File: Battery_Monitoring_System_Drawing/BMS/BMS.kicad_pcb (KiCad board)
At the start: 2 copper layers, 62 parts, among them J1 SWD Pins, J2 INPUT 5V, J3 Micro_SD_Card_Det_Hirose_DM3AT, J4 Conn_01x04, J5 ACS INPUT, SW1 SW_Push_Dual, SW2 ESP RESET BUTTON, U1 STM32F101C8Tx, U2 AMS1117-3.3, U3 AMS1117-3.3, U4 ESP-12E, U5 ACS712xLCTR-30A, Y1 8M, Y2 32K

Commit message: Layout çizimi tamanlandı.
Layout çizimi ilk şablonu tamamlandı.
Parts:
- removed D4: SD CARD LED, LED_SMD:LED_0805_2012Metric
- removed R17: 68K, Resistor_SMD:R_0805_2012Metric
- C10, C14, C16, C18, C20, C21, C6, C7, C9, D3, J3, R13, R15, R2, R4, R5, R7, R8, R9, U2, U3: moved to B.Cu
- C19: value 100nF -> 10uF; moved to B.Cu
- C22: value 1nF -> 100nF
- C23: value 10uF -> 1nF
- J5: footprint Connector_Phoenix_MSTB:PhoenixContact_MSTBA_2,5_2-G_1x02_P5.00mm_Horizontal -> TerminalBlock_Phoenix:TerminalBlock_Phoenix_MKDS-1,5-2_1x02_P5.00mm_Horizontal
- R10: value 10K -> 12K; moved to B.Cu
- R11: value 12K -> 3.3K; moved to B.Cu
- R12: value 3.3K -> 12K; moved to B.Cu
- R14: value 12K -> 22K; moved to B.Cu
- R16: value 22K -> 68K; moved to B.Cu
- R6: value 470 -> 10K; moved to B.Cu
- Y1: footprint Crystal:Crystal_SMD_HC49-SD_HandSoldering -> Crystal:Crystal_SMD_HC49-SD
- moved R15 89.3 mm to (140.2, 105.4), turned to 180 degrees
- moved R16 85.1 mm to (140.2, 107.4)
- moved R12 79.4 mm to (143.6, 105.4), turned to 180 degrees
- moved TH1 72.0 mm to (155.7, 111.3), turned to 180 degrees
- moved R11 70.8 mm to (147.1, 107.4)
- moved JP3 67.0 mm to (151.9, 105.4), turned to 90 degrees
- moved R14 61.7 mm to (143.6, 107.4)
- moved R13 61.1 mm to (152.5, 108.8)
- moved J3 59.1 mm to (160.1, 87.9), turned to 270 degrees
- moved J5 58.5 mm to (162.1, 109.1)
- moved C21 58.4 mm to (177.0, 101.9), turned to 180 degrees
- moved SW2 58.2 mm to (171.0, 108.1)
- moved J4 54.5 mm to (146.8, 111.3), turned to 180 degrees
- moved D1 53.1 mm to (129.2, 104.1)
- moved U5 52.0 mm to (157.2, 98.6), turned to 90 degrees
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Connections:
- C20 pad 1: /ESP_RST -> +3.3VA
- C21 pad 1: GND -> /ESP_RST
- C21 pad 2: /Analog_Measurements/ACS_SUPPLY -> GND
- C22 pad 1: Net-(C22-Pad1) -> GND
- C22 pad 2: GND -> ACS_SUPPLY
- C23 pad 1: +3.3VA -> Net-(C23-Pad1)
- J3 pad 4: +3V3 -> +3.3VA
- JP3 pad 2: /Analog_Measurements/ACS_SUPPLY -> ACS_SUPPLY
- R10 pad 1: +3V3 -> CELL_3
- R10 pad 2: /SD_MOSI -> GND
- R11 pad 1: /Analog_Measurements/CELL_3 -> Net-(J4-Pad2)
- R11 pad 2: GND -> CELL_3
- R12 pad 1: Net-(J4-Pad2) -> CELL_2
- R12 pad 2: /Analog_Measurements/CELL_3 -> GND
- R13 pad 2: /Analog_Measurements/NTC -> NTC
- R14 pad 1: /Analog_Measurements/CELL_2 -> Net-(J4-Pad3)
- R14 pad 2: GND -> CELL_2
- R15 pad 1: Net-(J4-Pad3) -> CELL_1
- R15 pad 2: /Analog_Measurements/CELL_2 -> GND
- R16 pad 1: /Analog_Measurements/CELL_1 -> Net-(J4-Pad4)
- R16 pad 2: GND -> CELL_1
- R6 pad 2: Net-(D4-Pad2) -> /SD_MOSI
- R7 pad 1: +3V3 -> +3.3VA
- R7 pad 2: Net-(J3-Pad8) -> /SD_SCLK
- R8 pad 1: +3V3 -> +3.3VA
- R9 pad 1: +3V3 -> +3.3VA
- R9 pad 2: /SD_SCLK -> Net-(J3-Pad8)
- TH1 pad 1: /Analog_Measurements/NTC -> NTC
- U4 pad 3: +3.3VA -> +3V3
- U4 pad 8: +3.3VA -> +3V3
- U5 pad 6: Net-(C22-Pad1) -> Net-(C23-Pad1)
- U5 pad 7: /Analog_Measurements/ACS_OUT -> ACS_OUT
- U5 pad 8: /Analog_Measurements/ACS_SUPPLY -> ACS_SUPPLY
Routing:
- net +3V3: track 0.00 -> 146.5 mm, vias 0 -> 7
- net GND: track 0.00 -> 73.8 mm, vias 0 -> 48
- net +3.3VA: track 0.00 -> 55.8 mm
- net +5V: track 0.00 -> 53.7 mm
- net /ESP_RST: track 0.00 -> 35.7 mm, vias 0 -> 1
- net NRST: track 0.00 -> 33.0 mm, vias 0 -> 1
- net Net-(J3-Pad8): track 0.00 -> 32.8 mm
- net ESP_TX: track 0.00 -> 31.2 mm, vias 0 -> 2
- net NTC: track 0.00 -> 30.5 mm, vias 0 -> 1
- net ESP_RX: track 0.00 -> 28.4 mm, vias 0 -> 2
- net TEST_PIN: track 0.00 -> 25.1 mm
- net CELL_1: track 0.00 -> 22.7 mm, vias 0 -> 1
- net SWDIO: track 0.00 -> 22.5 mm, vias 0 -> 1
- net /SD_MISO: track 0.00 -> 21.9 mm, vias 0 -> 1
- net CELL_2: track 0.00 -> 20.3 mm, vias 0 -> 1
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- added copper zone on B.Cu, net GND
- added copper zone on F.Cu, net GND
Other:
- board outline added: 52.6 x 41.4 mm
- rule via_min_size: 0.4 -> 0.3

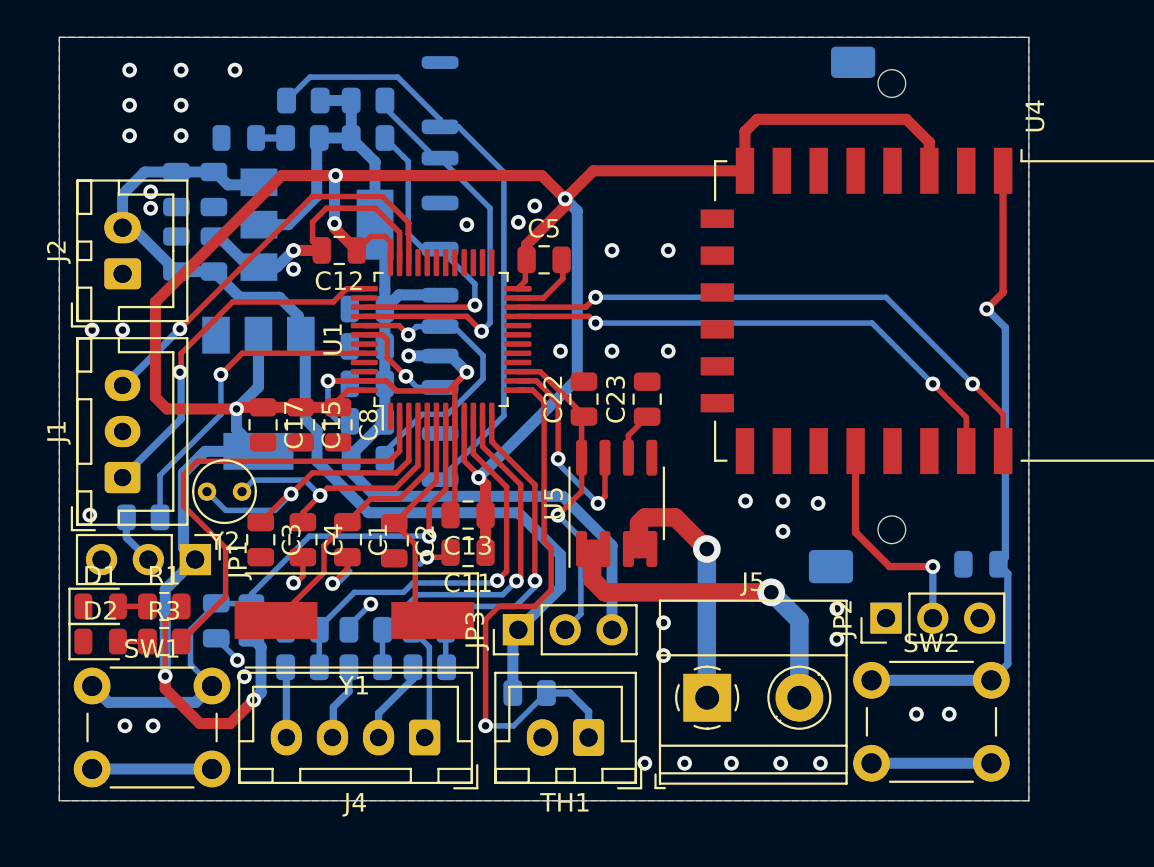
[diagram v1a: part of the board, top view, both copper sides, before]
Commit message: DRC hataları çözüldü.
DRC hataları çözüldü ve SD Card 3D görüntüsü eklendi.
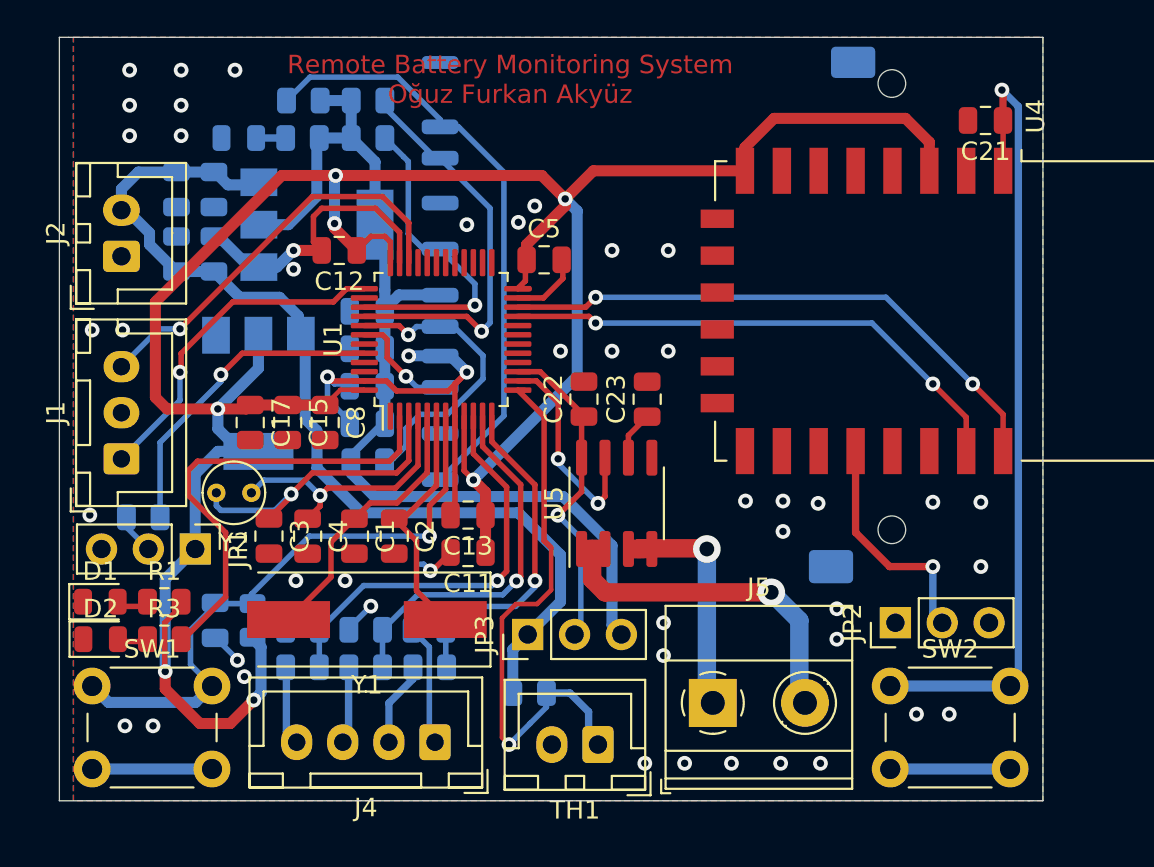
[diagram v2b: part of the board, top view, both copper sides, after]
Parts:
- C21: moved to F.Cu
- moved C21 24.1 mm to (177.2, 77.8)
- moved SW2 1.06 mm to (172.1, 108.5)
- moved J1 1.02 mm to (130.4, 96.1)
- moved J2 0.95 mm to (130.4, 85.2)
- moved C15 0.71 mm to (139.4, 94.2)
- moved C17 0.71 mm to (137.4, 94.2)
- moved C8 0.71 mm to (141.4, 94.2)
- moved Y1 0.68 mm to (143.7, 104.9)
- moved TH1 0.64 mm to (156.2, 111.6)
- moved J4 0.61 mm to (147.4, 111.5)
- moved JP1 0.57 mm to (134.4, 101.0)
- moved JP3 0.57 mm to (152.4, 105.7)
- moved JP2 0.57 mm to (172.3, 105.0)
- moved Y2 0.51 mm to (137.4, 98.0)
- moved C3 0.49 mm to (138.4, 100.3)
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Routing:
- net /ESP_RST: track 35.7 -> 43.8 mm
- net GND: track 73.8 -> 69.8 mm, vias 48 -> 49
- net Net-(J5-Pad1): track 15.3 -> 13.1 mm
- net SWCLK: track 19.4 -> 18.4 mm
- net OSC32_OUT: track 15.3 -> 14.6 mm
- net /ESP_IO0: track 12.2 -> 12.8 mm
- net OSC32_IN: track 17.2 -> 16.6 mm
- net Net-(JP1-Pad2): track 2.85 -> 2.27 mm
- net NTC: track 30.5 -> 30.0 mm
- net OSC_OUT: track 12.9 -> 13.4 mm
- net +3.3VA: track 55.8 -> 56.3 mm
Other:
- board size 52.6 x 41.4 mm -> 53.3 x 41.4 mm
- board text added: "Remote Battery Monitoring System Oğuz Furkan Akyüz"

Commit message: Düzenleme yapıldı.
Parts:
- moved C17 1.78 mm to (135.6, 94.2)
- moved C15 1.78 mm to (137.6, 94.2)
- moved C8 1.78 mm to (139.6, 94.2)
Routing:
- net +3V3: track 146.3 -> 151.0 mm
- net BOOT0: track 17.4 -> 18.1 mm
- net GND: vias 49 -> 51
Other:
- board text added: "Oğuz Furkan Akyüz - 2021"
- board text added: "Remote Battery Monitoring System"
- board text removed: "Remote Battery Monitoring System Oğuz Furkan Akyüz"

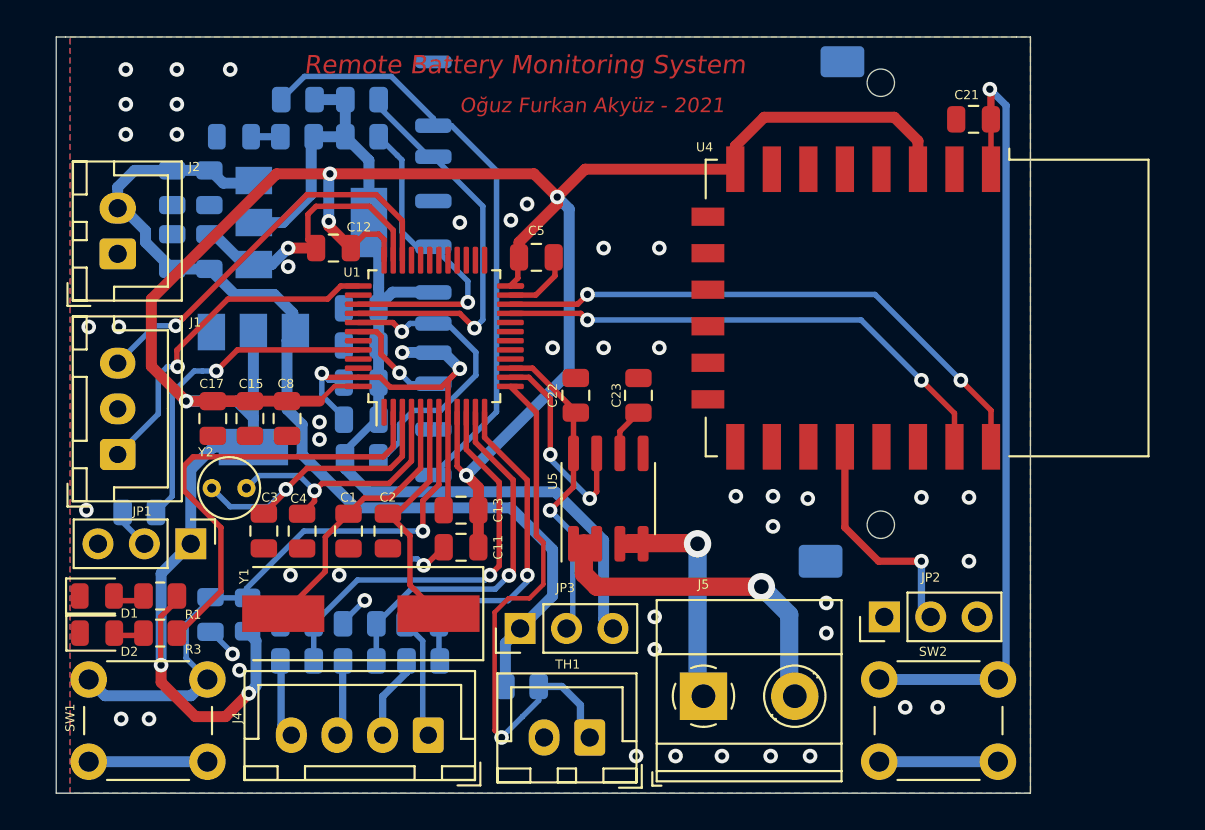
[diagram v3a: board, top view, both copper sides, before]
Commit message: Micro Sd kılıf eklendi.
Sd kart holder kılıfı micro sd kart soket kılıfı ile değiştirildi.
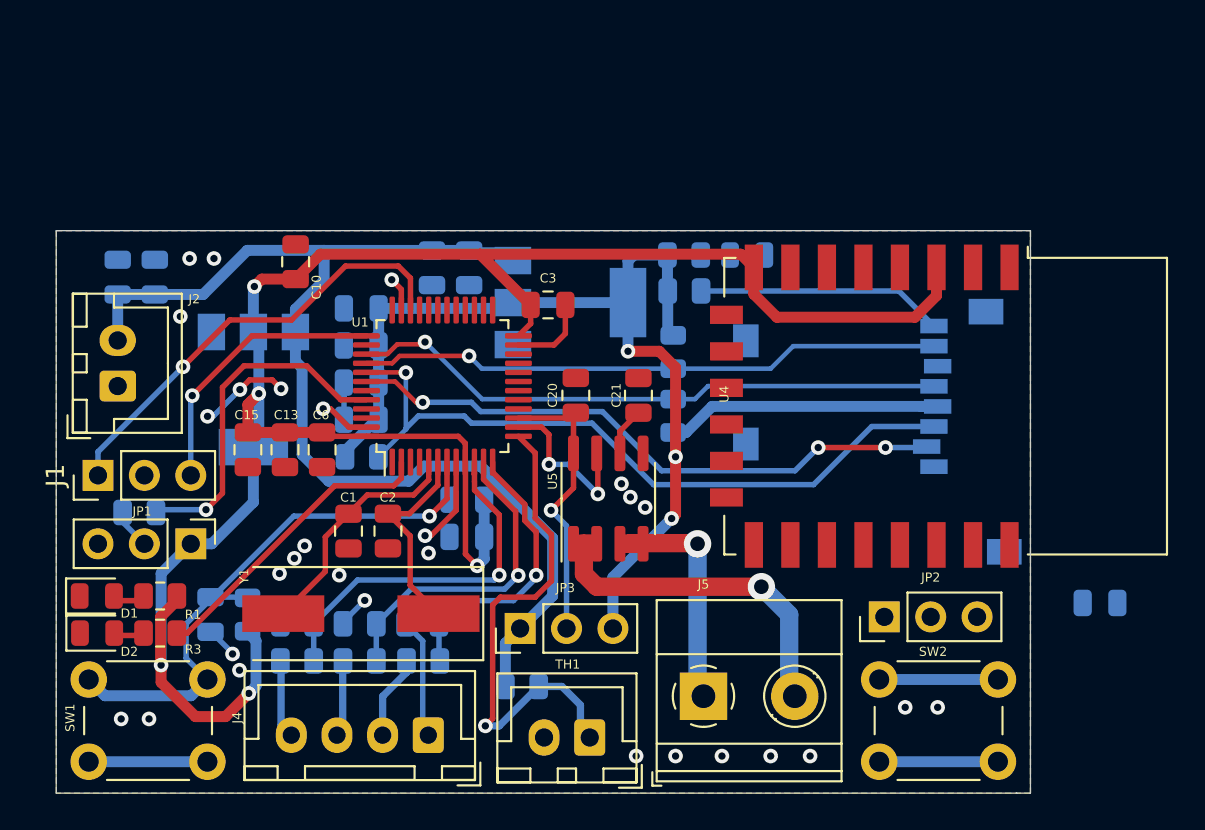
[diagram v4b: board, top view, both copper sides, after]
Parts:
- removed the C3 at (138.4, 100.3)
- removed the C4 at (140.5, 100.3)
- removed Y2: 32K, Crystal:Crystal_C38-LF_D3.0mm_L8.0mm_Vertical
- C11: renamed from C13; moved to B.Cu
- C19: renamed from C21; moved to B.Cu
- C9: renamed from C11; moved to B.Cu
- J1: footprint Connector_JST:JST_XH_B3B-XH-A_1x03_P2.50mm_Vertical -> Connector_PinHeader_2.54mm:PinHeader_1x03_P2.54mm_Vertical
- J3: value Micro_SD_Card_Det_Hirose_DM3AT -> 693071010811; footprint Connector_Card:SD_Kyocera_145638009511859+ -> micro_sd_8+1:micro_sd_8+1
- moved D3 28.8 mm to (164.8, 85.2), turned to 180 degrees
- moved C19 27.4 mm to (184.2, 104.3)
- moved R9 23.6 mm to (161.4, 87.2), turned to 0 degrees
- moved R7 22.9 mm to (160.8, 94.0), turned to 90 degrees
- moved R4 22.2 mm to (161.4, 85.2), turned to 180 degrees
- moved R8 21.9 mm to (160.8, 90.5), turned to 270 degrees
- moved C4 14.9 mm to (147.6, 85.9)
- moved C7 14.9 mm to (149.6, 85.9)
- moved U2 14.8 mm to (155.2, 87.8)
- moved J3 13.7 mm to (172.0, 94.9)
- moved J2 7.24 mm to (130.4, 92.4)
- moved U4 5.47 mm to (175.7, 93.5)
- moved C5 3.30 mm to (130.4, 86.4)
- moved C8 3.30 mm to (132.4, 86.4)
- moved U1 2.77 mm to (148.1, 92.4)
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- renumbered C12 to C10, C14 to C12, C15 to C13, C16 to C14, C17 to C15, C18 to C16, C19 to C17, C20 to C18, C22 to C20, C23 to C21, C5 to C3, C6 to C4, C7 to C5, C8 to C6, C9 to C7, C10 to C8
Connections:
- J1 pad 1: SWCLK -> SWDIO
- J1 pad 3: SWDIO -> SWCLK
- J3 pad 10: GND -> Net-(J3-Pad10)
- J3 pad 9: Net-(J3-Pad8) -> Net-(J3-Pad9)
- U1 pad 3: OSC32_IN -> Net-(U1-Pad3)
- U1 pad 4: OSC32_OUT -> Net-(U1-Pad4)
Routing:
- net +3V3: track 151.0 -> 112.1 mm, vias 7 -> 5
- net /ESP_RST: track 43.8 -> 6.50 mm, vias 1 -> 0
- net ESP_TX: track 31.2 -> 0.00 mm, vias 2 -> 0
- net ESP_RX: track 28.4 -> 0.00 mm, vias 2 -> 0
- net /SD_CS: track 5.87 -> 33.2 mm, vias 1 -> 3
- net GND: track 69.8 -> 44.4 mm, vias 51 -> 29
- net /SD_MOSI: track 16.4 -> 39.5 mm
- net Net-(J3-Pad8): track 32.8 -> 13.5 mm
- net OSC32_IN: track 16.2 -> 0.00 mm, vias 1 -> 0
- net /SD_SCLK: track 17.7 -> 32.9 mm
- net OSC32_OUT: track 14.6 -> 0.00 mm, vias 1 -> 0
- net +3.3VA: track 56.3 -> 69.4 mm, vias 0 -> 3
- net /ESP_IO0: track 12.8 -> 0.21 mm, vias 1 -> 0
- net /SD_MISO: track 21.9 -> 32.0 mm
- net +5V: track 54.4 -> 62.9 mm
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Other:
- board size 53.3 x 41.4 mm -> 53.3 x 30.8 mm
- board text removed: "Oğuz Furkan Akyüz - 2021"
- board text removed: "Remote Battery Monitoring System"

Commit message: Layout_v2 çizimi tamamlandı.
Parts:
- moved C19 14.6 mm to (169.8, 107.2), turned to 270 degrees
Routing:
- net ESP_TX: track 0.00 -> 34.6 mm, vias 0 -> 2
- net ESP_RX: track 0.00 -> 32.1 mm, vias 0 -> 2
- net /ESP_RST: track 6.50 -> 37.6 mm, vias 0 -> 1
- net /ESP_IO0: track 0.21 -> 10.4 mm, vias 0 -> 1
- net GND: track 44.4 -> 50.8 mm, vias 29 -> 31
- net Net-(J3-Pad8): track 13.5 -> 14.4 mm
- net +5V: track 62.9 -> 63.5 mm
- net +3V3: track 112.1 -> 111.6 mm

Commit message: Layout'da düzenlemeler yapıldı.
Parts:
- turned C10 to 270 degrees
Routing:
- net +3V3: track 111.6 -> 118.2 mm, vias 5 -> 7
- net GND: track 50.8 -> 52.5 mm, vias 31 -> 91
- net /SD_MISO: track 32.4 -> 33.8 mm
- net ESP_RX: track 32.1 -> 33.4 mm
- net SWDIO: track 24.6 -> 25.9 mm
- net ESP_TX: track 34.6 -> 35.8 mm

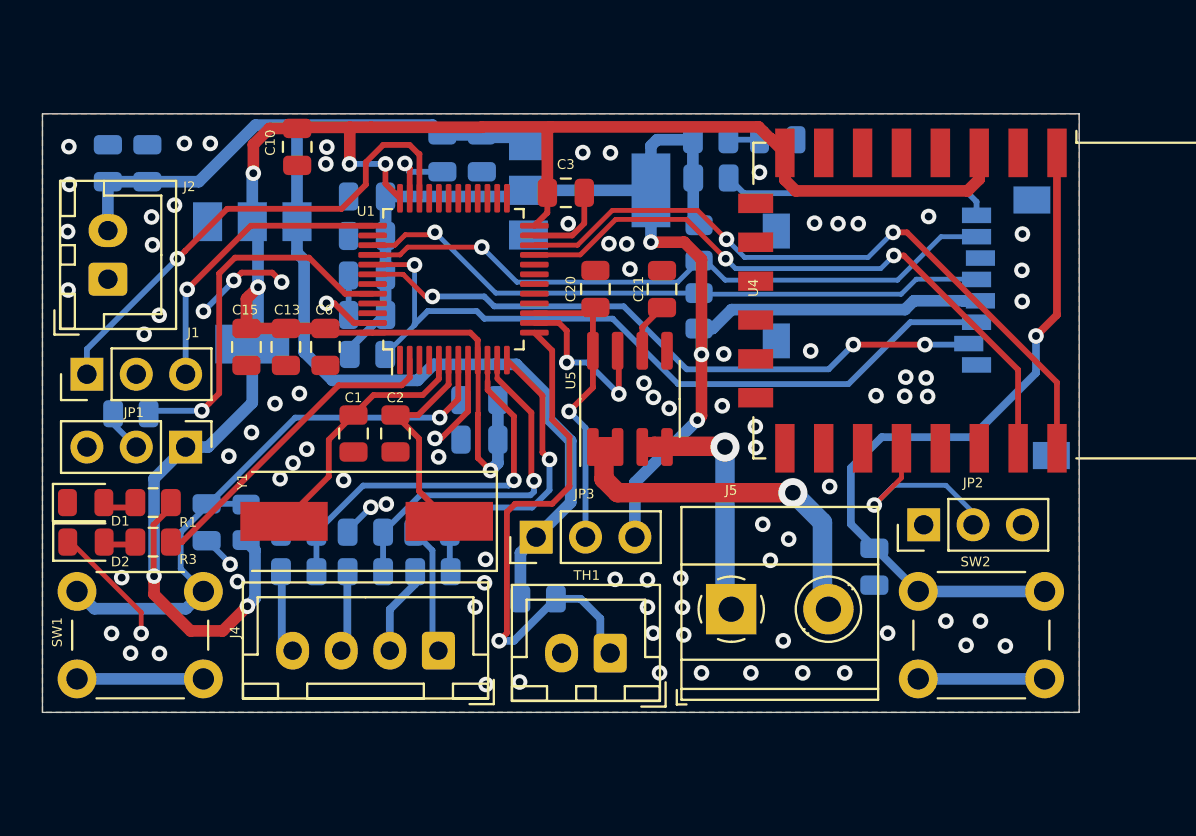
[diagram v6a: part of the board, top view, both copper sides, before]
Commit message: Çizim tamamlandı.
DRC yapıldı ve hatalar düzeltildi.
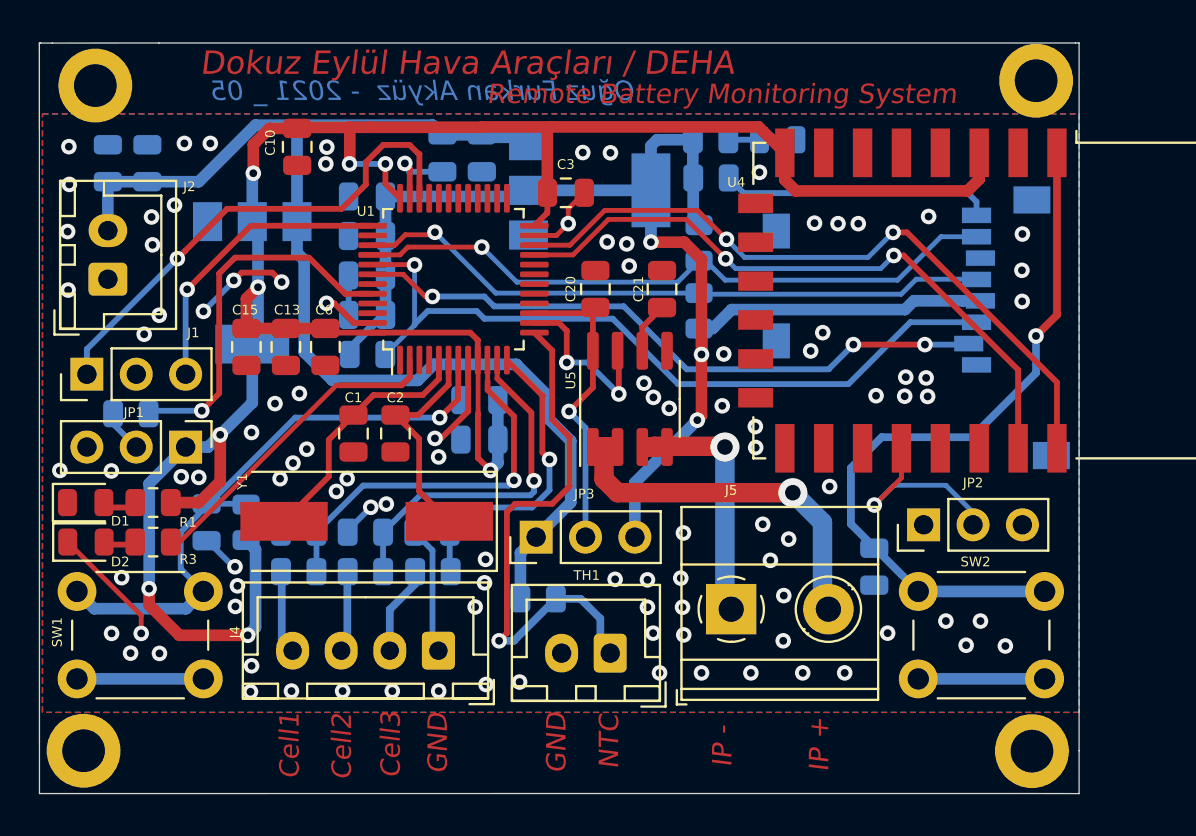
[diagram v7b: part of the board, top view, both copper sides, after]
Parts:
- added H1: Mounting_Hole, MountingHole:MountingHole_2.2mm_M2_DIN965_Pad, F.Cu at (129.7, 82.4)
- added H2: Mounting_Hole, MountingHole:MountingHole_2.2mm_M2_DIN965_Pad, F.Cu at (177.9, 116.7)
- added H3: Mounting_Hole, MountingHole:MountingHole_2.2mm_M2_DIN965_Pad, F.Cu at (129.1, 116.7)
- added H4: Mounting_Hole, MountingHole:MountingHole_2.2mm_M2_DIN965_Pad, F.Cu at (178.1, 82.2)
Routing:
- net +3V3: track 118.2 -> 121.4 mm, vias 7 -> 8
- net GND: track 52.5 -> 52.0 mm, vias 91 -> 105
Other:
- board size 53.3 x 30.8 mm -> 53.5 x 38.6 mm
- board text added: "Cell1"
- board text added: "Cell2"
- board text added: "Cell3"
- board text added: "Dokuz Eylül Hava Araçları / DEHA"
- board text added: "GND"
- board text added: "IP +"
- board text added: "IP -"
- board text added: "NTC"
- board text added: "Oğuz Furkan Akyüz - 2021 _ 05"
- board text added: "Remote Battery Monitoring System"
